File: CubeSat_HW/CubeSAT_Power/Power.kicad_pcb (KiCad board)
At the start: 2 copper layers, 64.7 x 56 mm, 12 parts, among them J1 USB_B_Micro, J2 Conn_01x02_Pin, J4 Conn_02x20_Odd_Even, Q1 AO3401A, Q2 AO3401A, U1 LM1117MP-5.0

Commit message: feat: Added new version for the Power Supply Board
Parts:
- added D1: 12V, Diode_SMD:D_SOD-123, F.Cu at (146.6, 106.8)
- added R1: 10k, Resistor_SMD:R_0603_1608Metric, F.Cu at (148.6, 106.0)
- added R2: 10R, Resistor_SMD:R_0603_1608Metric, F.Cu at (151.1, 105.2)
- Q2: value AO3401A -> IRLML2502
- moved C1 0.89 mm to (135.0, 92.9)
- moved Q2 0.76 mm to (143.6, 106.4), turned to -90 degrees
- moved J4 0.14 mm to (126.9, 70.1)
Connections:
- Q2 pad 1: GND -> Net-(D1-K)
- Q2 pad 3: /COMMAND -> GND
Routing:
- net /COMMAND: track 53.6 -> 45.0 mm
- net Net-(D1-K): track 0.00 -> 5.85 mm
- net GND: track 41.2 -> 43.0 mm, vias 16 -> 97
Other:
- outline, holes or cut-outs redrawn
- board text added: "CubeSAT Power Supply Rev 0.0"
- board text removed: "CUBESAT Power Supply Rev 0.0"

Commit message: fix: Minor fixes to the Power Supply Board
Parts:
- removed D1: 12V, Diode_SMD:D_SOD-123
- added Q3: IRLM2502, Package_TO_SOT_SMD:SOT-23, F.Cu at (142.9, 105.0)
- added R3: 100k, Resistor_SMD:R_0603_1608Metric, F.Cu at (143.5, 111.4)
- added R4: 100k, Resistor_SMD:R_0603_1608Metric, F.Cu at (141.8, 111.4)
- added R5: 100k, Resistor_SMD:R_0603_1608Metric, F.Cu at (142.9, 102.2)
- added REF**: ESD-Logo_6.6x6mm_SilkScreen, Symbol:ESD-Logo_6.6x6mm_SilkScreen, F.Cu at (127.7, 105.6)
- Q2: value IRLML2502 -> 2N7002
- R1: value 10k -> 1k
- R2: value 10R -> 100k
- moved Q2 3.60 mm to (146.8, 104.8), turned to 180 degrees
- moved R1 3.60 mm to (152.0, 104.6), turned to 0 degrees
- moved C1 2.16 mm to (135.0, 90.7)
- moved C2 2.16 mm to (138.0, 99.8)
- moved U1 2.16 mm to (140.8, 89.8)
- moved R2 1.60 mm to (149.5, 104.7), turned to 90 degrees
- moved J1 1.49 mm to (142.0, 115.8)
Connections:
- C2 pad 1: /VOut -> Net-(Q3-S)
- J1 pad 1: /VOut -> Net-(J1-VBUS)
- J1 pad 2: unconnected-(J1-D--Pad2) -> Net-(J1-D-)
- J1 pad 3: unconnected-(J1-D+-Pad3) -> Net-(J1-D+)
- Q2 pad 1: Net-(D1-K) -> Net-(Q2-G)
- Q2 pad 2: /VOut -> GND
- Q2 pad 3: GND -> Net-(Q2-D)
- R1 pad 1: Net-(D1-K) -> Net-(Q2-G)
- R1 pad 2: GND -> /COMMAND
- R2 pad 1: /COMMAND -> Net-(Q2-G)
- R2 pad 2: Net-(D1-K) -> GND
- U1 pad 2: /VOut -> Net-(Q3-S)
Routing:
- net (no net): track 0.00 -> 33.9 mm
- net /VOut: track 32.5 -> 0.00 mm, vias 42 -> 0
- net /COMMAND: track 45.0 -> 32.4 mm
- net Net-(D1-K): track 5.85 -> 0.00 mm
- net Net-(J1-D+): track 0.00 -> 2.86 mm
- net Net-(J1-D-): track 0.00 -> 2.32 mm
- net GND: track 43.0 -> 41.5 mm, vias 97 -> 15
- net Net-(Q1-S): track 9.85 -> 8.97 mm
- net Net-(Q3-S): vias 0 -> 42
- added copper zone on B.Cu, net Net-(Q3-S)
- added copper zone on F.Cu, net Net-(Q3-S)
- removed copper zone on B.Cu, net /VOut
- removed copper zone on F.Cu, net /VOut
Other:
- outline, holes or cut-outs redrawn

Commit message: release: Added version II of PS project.
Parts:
- removed J1: USB_B_Micro, Connector_USB:USB_Micro-B_GCT_USB3076-30-A
- added J3: USB_A, Connector_USB:USB_A_CNCTech_1001-011-01101_Horizontal, F.Cu at (142.5, 119.2)
- moved R3 5.81 mm to (139.8, 106.8), turned to 0 degrees
- moved R4 4.68 mm to (142.9, 106.8), turned to 180 degrees
- moved Q3 3.17 mm to (146.1, 105.6)
- moved R5 3.17 mm to (146.0, 102.9)
- moved Q2 3.11 mm to (149.8, 105.4)
- moved R2 3.10 mm to (152.6, 105.3)
- moved R1 2.28 mm to (154.1, 105.3), turned to 90 degrees
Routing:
- net (no net): track 33.9 -> 0.00 mm
- net Net-(Q3-S): track 0.00 -> 28.0 mm
- net GND: track 41.5 -> 23.3 mm, vias 15 -> 71
- net /COMMAND: track 32.4 -> 42.1 mm
- net Net-(Q2-D): track 0.00 -> 4.06 mm
- net Net-(Q2-G): track 0.00 -> 3.47 mm
- net Net-(J3-VBUS): track 0.00 -> 2.99 mm
- net Net-(J3-D-): track 2.32 -> 3.35 mm
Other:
- outline, holes or cut-outs redrawn
- board text added: "CubeSAT Power Supply Rev 1.0"
- board text removed: "CubeSAT Power Supply Rev 0.0"

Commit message: feat: Added new version for HW Board
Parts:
- moved R3 1.09 mm to (139.8, 105.7)
- moved J3 1.08 mm to (142.5, 118.1)
- moved R4 1.07 mm to (142.8, 105.7)
- moved Q2 1.01 mm to (149.8, 104.4)
- moved R5 1.01 mm to (146.0, 101.9)
- moved Q3 1.01 mm to (146.1, 104.6)
- moved R2 0.81 mm to (152.6, 104.5)
- moved R1 0.78 mm to (154.1, 104.5)
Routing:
- net /COMMAND: track 42.1 -> 41.3 mm
- net Net-(Q3-S): track 28.0 -> 27.8 mm, vias 42 -> 44
- net GND: vias 71 -> 11

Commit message: fix: Small changes
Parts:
- removed J4: Conn_02x20_Odd_Even, Connector_PinHeader_2.54mm:PinHeader_2x20_P2.54mm_Vertical
- added J1: USB_B_Micro, Connector_USB:USB_Micro-B_GCT_USB3076-30-A, F.Cu at (142.2, 117.4)
- J3: value USB_A -> Conn_02x17_Odd_Even; footprint Connector_USB:USB_A_CNCTech_1001-011-01101_Horizontal -> Connector_IDC:IDC-Header_2x17_P2.54mm_Horizontal
- moved J3 47.5 mm to (130.7, 72.1), turned to 90 degrees
- moved R3 8.37 mm to (144.1, 112.9), turned to -90 degrees
- moved R4 7.18 mm to (142.3, 112.9), turned to -90 degrees
- moved Q3 5.89 mm to (140.9, 107.5)
- moved R5 5.57 mm to (140.9, 104.2)
- moved Q2 5.55 mm to (144.7, 106.6)
- moved R1 5.55 mm to (149.0, 106.8)
- moved R2 5.55 mm to (147.5, 106.7)
- moved C2 0.38 mm to (138.0, 99.5)
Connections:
- J3 pad 1: Net-(J3-VBUS) -> +3.3V
- J3 pad 2: Net-(J3-D-) -> +3.3V
- J3 pad 3: Net-(J3-D+) -> GND
- J3 pad 5: GND -> /SDA
- Q3 pad 3: Net-(J3-VBUS) -> Net-(J1-VBUS)
- R3 pad 2: Net-(J3-D+) -> Net-(J1-D+)
- R4 pad 2: Net-(J3-D-) -> Net-(J1-D-)
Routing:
- net GND: track 23.3 -> 44.9 mm, vias 11 -> 86
- net /COMMAND: track 41.3 -> 53.5 mm
- net Net-(J1-VBUS): track 0.00 -> 7.69 mm
- net Net-(J1-D+): track 0.00 -> 3.42 mm
- net Net-(J3-D-): track 3.36 -> 0.00 mm
- net Net-(J3-D+): track 3.11 -> 0.00 mm
- net Net-(J3-VBUS): track 2.99 -> 0.00 mm
- net /SDA: track 0.00 -> 2.54 mm
- net /SCL: track 0.00 -> 2.54 mm
- net /SCK: track 0.00 -> 2.54 mm
- net /PWM1: track 0.00 -> 2.54 mm
- net /PWM0: track 0.00 -> 2.54 mm
- net /MOSI: track 0.00 -> 2.54 mm
- net /MISO: track 0.00 -> 2.54 mm
- net /LED_2: track 0.00 -> 2.54 mm
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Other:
- outline, holes or cut-outs redrawn

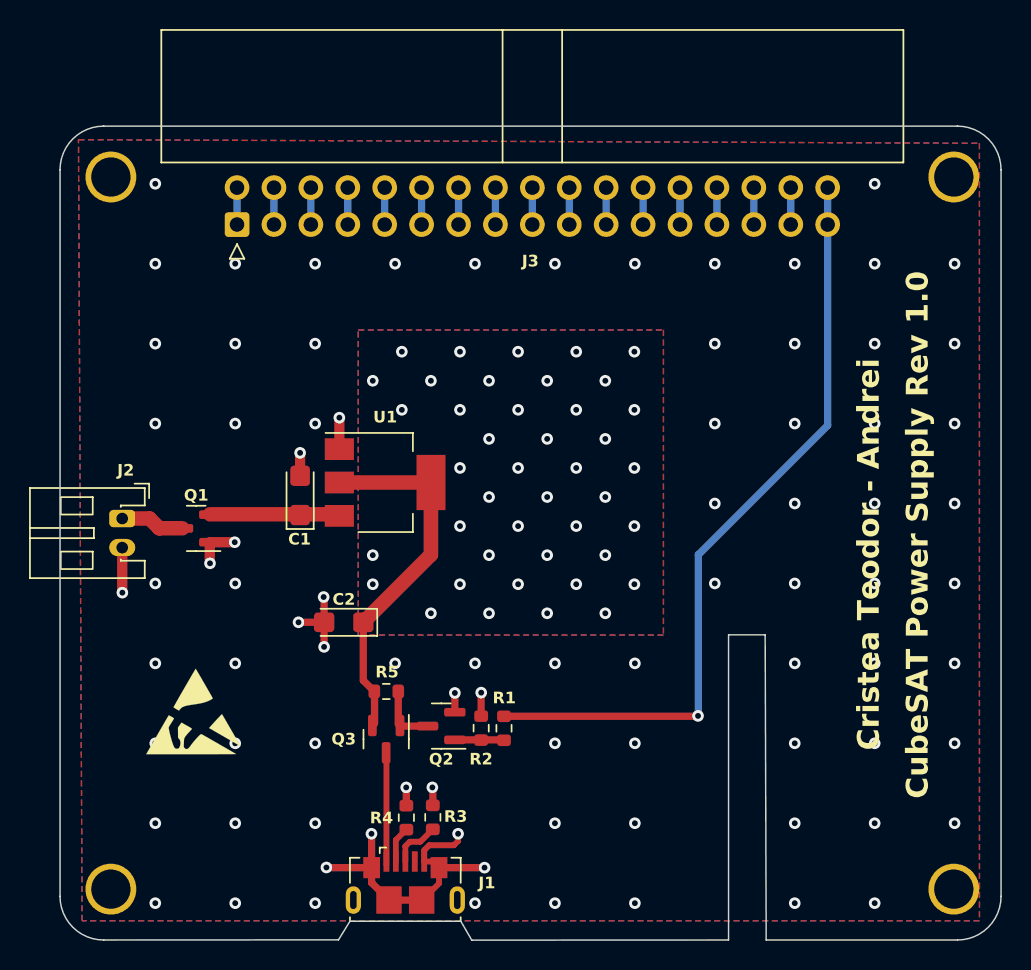
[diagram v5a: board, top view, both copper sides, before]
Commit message: feat: Added Payload Board and new Gerbers for the project
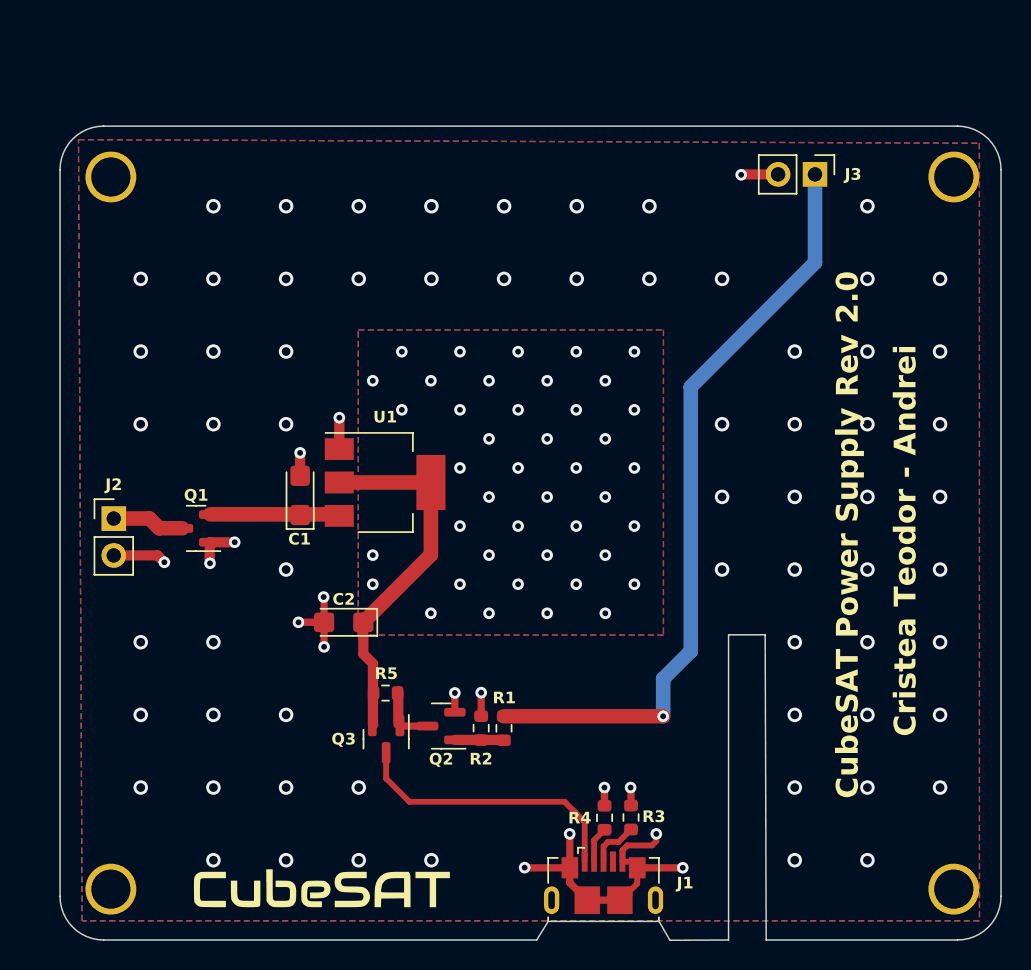
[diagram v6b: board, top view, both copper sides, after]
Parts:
- removed REF**: ESD-Logo_6.6x6mm_SilkScreen, Symbol:ESD-Logo_6.6x6mm_SilkScreen
- added G***: LOGO, Logo:Logo, F.Cu at (136.5, 117.7)
- J2: footprint Connector_TE-Connectivity:TE_440055-2_1x02_P2.00mm_Horizontal -> Connector_PinHeader_2.54mm:PinHeader_1x02_P2.54mm_Vertical
- J3: value Conn_02x17_Odd_Even -> Conn_01x02_Pin; footprint Connector_IDC:IDC-Header_2x17_P2.54mm_Horizontal -> Connector_PinHeader_2.54mm:PinHeader_1x02_P2.54mm_Vertical
- Q3: value IRLM2502 -> IRLML6402
- moved J3 39.9 mm to (170.4, 68.6), turned to -90 degrees
- moved R3 13.6 mm to (157.8, 112.9)
- moved J1 13.6 mm to (155.9, 117.4)
- moved R4 13.6 mm to (155.9, 112.9)
- moved J2 0.58 mm to (122.2, 92.3), turned to 0 degrees
- moved R5 0.12 mm to (140.9, 104.3)
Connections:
- J3 pad 1: +3.3V -> /COMMAND
- J3 pad 2: +3.3V -> GND
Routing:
- net Net-(J1-VBUS): track 7.69 -> 19.4 mm
- net /SDA: track 2.54 -> 0.00 mm
- net /SCL: track 2.54 -> 0.00 mm
- net /SCK: track 2.54 -> 0.00 mm
- net /PWM1: track 2.54 -> 0.00 mm
- net /PWM0: track 2.54 -> 0.00 mm
- net /MOSI: track 2.54 -> 0.00 mm
- net /MISO: track 2.54 -> 0.00 mm
- net /LED_2: track 2.54 -> 0.00 mm
- net /LED_1: track 2.54 -> 0.00 mm
- net /LED5: track 2.54 -> 0.00 mm
- net /LED4: track 2.54 -> 0.00 mm
- net /LED3: track 2.54 -> 0.00 mm
- net /CSN: track 2.54 -> 0.00 mm
- net /CE: track 2.54 -> 0.00 mm
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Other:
- outline, holes or cut-outs redrawn
- board text added: "CubeSAT Power Supply Rev 2.0"
- board text removed: "CubeSAT Power Supply Rev 1.0"
